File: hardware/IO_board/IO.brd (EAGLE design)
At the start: 167.9 x 122.5 mm, 73 parts, among them IC1 MAX232, IC10 74HCT245DW, IC11 74LVC1G08DBV, IC4 74HCT139N, IC5 74AC06N, IC7 MAX232, IC8 74HCT245DW, IC9 74HCT245DW, J1 DIN5, T1 BC847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

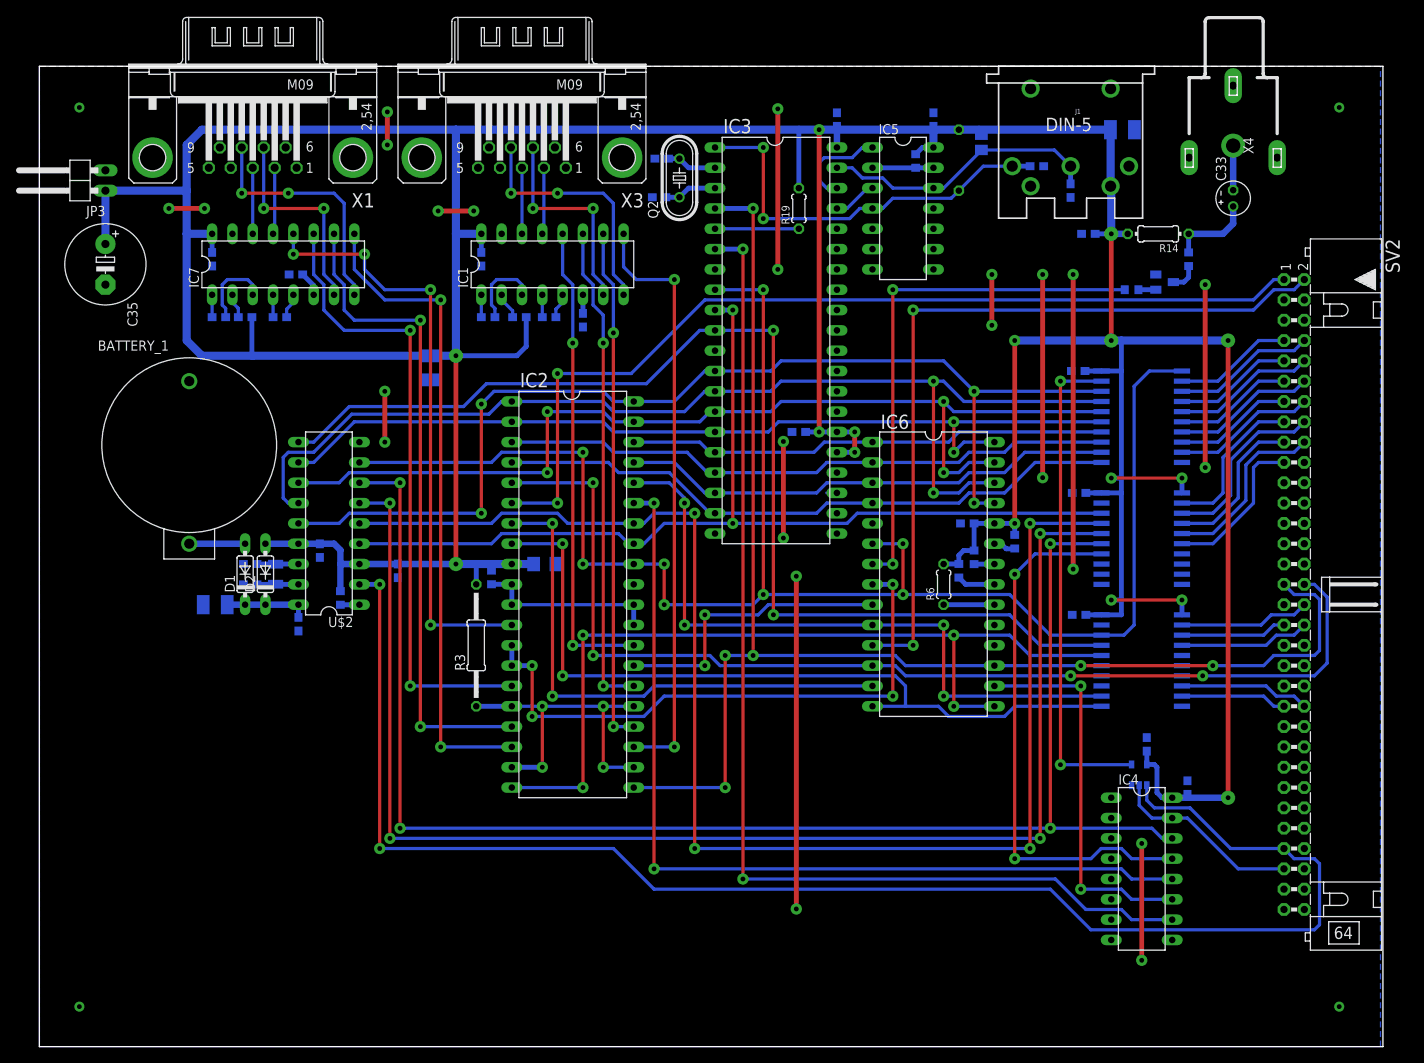
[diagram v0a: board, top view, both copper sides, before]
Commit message: Separate baudrate generator on I/O board
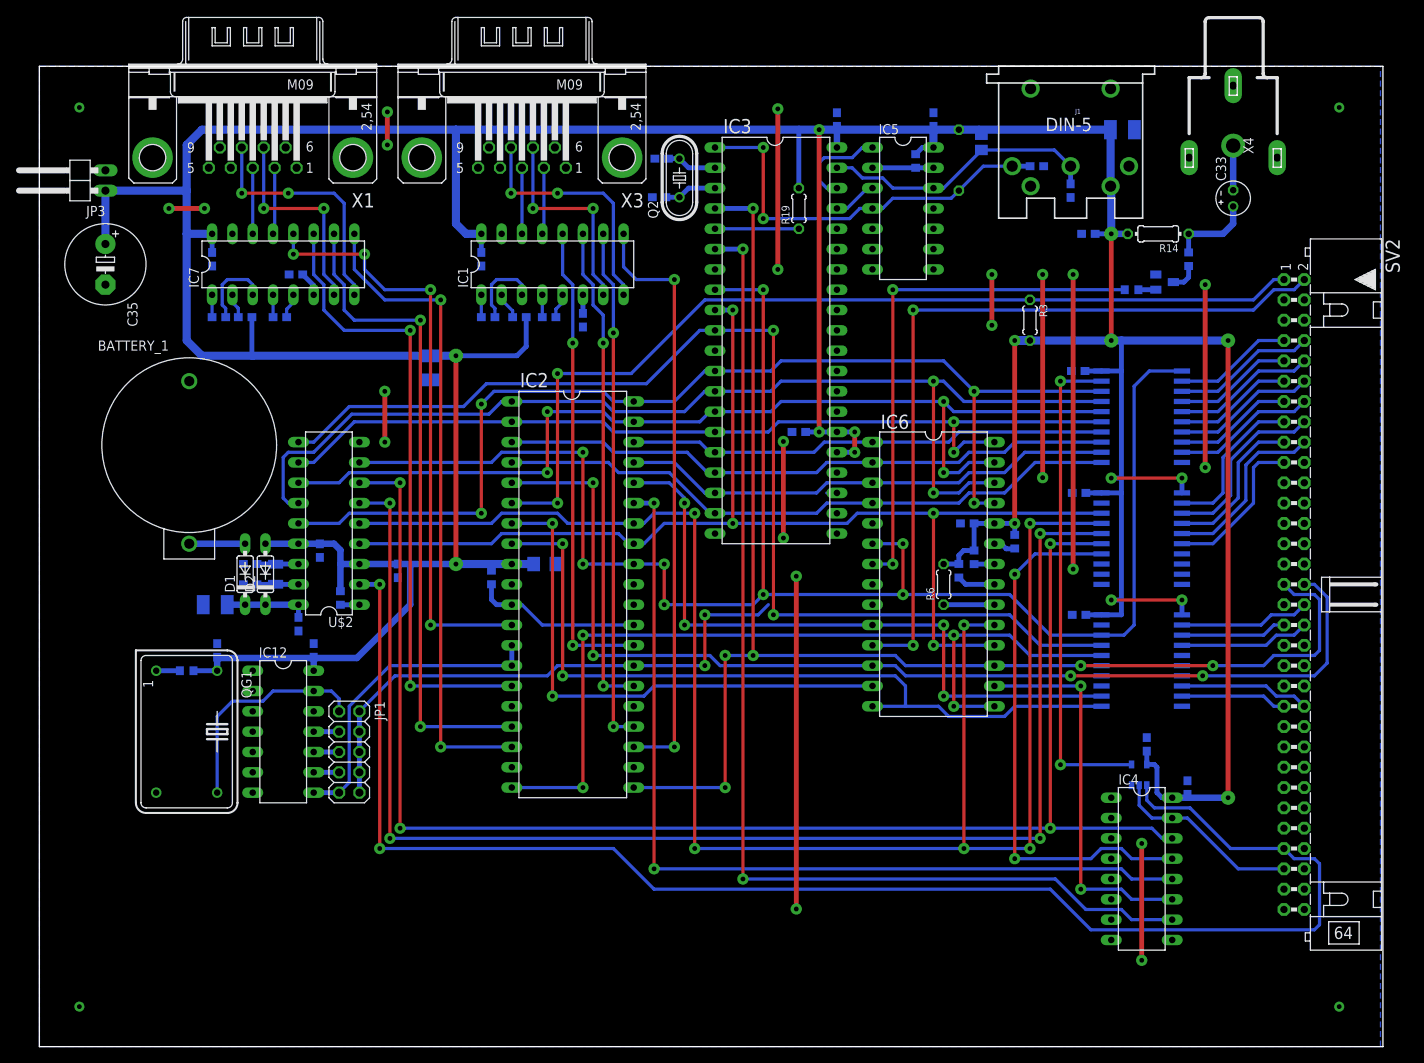
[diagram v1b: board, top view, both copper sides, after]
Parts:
- added C36, C37: 100N, rcl:C0603
- added IC12: 74HCT393N, 74xx-eu:DIL14
- added JP1: (no value), pinhead:2X05
- added QG1: (no value), crystal:DIL14S
- added R12: (no value), rcl:R0603
- R3: device rcl:0207/15 -> rcl:0204/5
- moved R3 80.3 mm to (123.8, 90.8), turned to 270 degrees
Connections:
- removed net BAUDRATE_A: IC2.13, IC2.14, IC6.8
- new net 1228800HZ: IC12.11, JP1.3
- new net 153600HZ: IC12.8, IC2.13, IC2.14, JP1.9
- new net 2457600HZ: IC12.13, JP1.1, QG1.8
- new net 307200HZ: IC12.9, JP1.7
- new net 614400HZ: IC12.10, JP1.5
- net A0: now also IC6.18
- net A1: now also IC6.19
- net BAUDRATE_B: now also JP1.10, JP1.2, JP1.4, JP1.6, JP1.8; no longer IC6.9
- net GND: now also C36.2, C37.2, IC12.1, IC12.12, IC12.2, IC12.7, IC2.19, IC2.22, QG1.7
- net IEI: now also R3.1
- net N$34: now also QG1.1, R12.2; no longer IC2.16, IC2.19, IC2.22, IC2.25, R3.1
- net N$36: no longer IC2.10, IC2.30
- net VCC: now also C36.1, C37.1, IC12.14, QG1.14, R12.1
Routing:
- net BAUDRATE_A: track 74.1 -> 0.00 mm, vias 4 -> 0
- net N$34: track 42.5 -> 2.96 mm, vias 4 -> 0
- net 153600HZ: track 0.00 -> 39.5 mm
- net BAUDRATE_B: track 36.7 -> 70.5 mm
- net A1: track 176.9 -> 208.6 mm, vias 4 -> 6
- net 2457600HZ: track 0.00 -> 28.1 mm
- net A0: track 124.3 -> 148.4 mm, vias 2 -> 4
- net VCC: track 622.2 -> 643.9 mm
- net GND: track 199.1 -> 194.7 mm, vias 24 -> 22
- net 614400HZ: track 0.00 -> 3.18 mm
- net 307200HZ: track 0.00 -> 3.18 mm
- net 1228800HZ: track 0.00 -> 3.18 mm
- net N$36: track 22.9 -> 21.0 mm

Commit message: I/O board: 0R resistors added to set baudrate at DART channel A
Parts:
- added R13: (no value), rcl:R0603
- added R16, R17, R18, R20, R21: 0R, rcl:R0603
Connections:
- new net BAUDRATE_A: IC2.13, IC2.14, R16.2, R17.2, R18.2, R20.2, R21.2
- new net N$41: IC12.2, R13.2
- net 1228800HZ: now also R17.1
- net 153600HZ: now also R21.1; no longer IC2.13, IC2.14
- net 2457600HZ: now also R16.1
- net 307200HZ: now also R20.1
- net 614400HZ: now also R18.1
- net GND: no longer IC12.2
- net VCC: now also R13.1
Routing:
- net BAUDRATE_A: track 0.00 -> 55.0 mm
- net 153600HZ: track 39.5 -> 5.18 mm
- net GND: track 194.7 -> 202.3 mm, vias 22 -> 24
- net N$41: track 0.00 -> 5.41 mm
- net 614400HZ: track 3.18 -> 5.18 mm
- net 307200HZ: track 3.18 -> 5.18 mm
- net 1228800HZ: track 3.18 -> 5.18 mm
- net 2457600HZ: track 28.1 -> 28.6 mm
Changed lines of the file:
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@@
 <element name="C37" library="rcl" package="C0603" value="100N" x="34.29" y="49.53" rot="MR90"/>
 <element name="R12" library="rcl" package="R0603" value="" x="18.415" y="46.99" rot="MR0"/>
+<element name="R13" library="rcl" package="R0603" value="" x="31.115" y="47.625" rot="MR270"/>
+<element name="R17" library="rcl" package="R0603" value="0R" x="31.4325" y="39.37" rot="MR0"/>
+<element name="R18" library="rcl" package="R0603" value="0R" x="31.4325" y="36.83" rot="MR0"/>
+<element name="R20" library="rcl" package="R0603" value="0R" x="31.4325" y="34.29" rot="MR0"/>
+<element name="R21" library="rcl" package="R0603" value="0R" x="31.4325" y="31.75" rot="MR0"/>
+<element name="R16" library="rcl" package="R0603" value="0R" x="38.1" y="44.45" rot="MR180"/>
 </elements>
 <signals>
@@
 <contactref element="IC12" pad="7"/>
 <contactref element="IC12" pad="12"/>
-<contactref element="IC12" pad="2"/>
 <contactref element="QG1" pad="7"/>
 <contactref element="IC12" pad="1"/>
 <contactref element="C36" pad="2"/>
 <contactref element="C37" pad="2"/>
+<via x="53.975" y="50.165" extent="1-16" drill="0.6" diameter="1.4224" shape="octagon"/>
+<via x="53.975" y="42.545" extent="1-16" drill="0.6" diameter="1.4224" shape="octagon"/>
+<wire x1="53.975" y1="50.165" x2="53.975" y2="42.545" width="0.6096" layer="1"/>
 </signal>
 <signal name="N$37">
@@
 <contactref element="C28" pad="1"/>
 <contactref element="C27" pad="2"/>
-<contactref element="IC2" pad="9"/>
 <wire x1="52.07" y1="114.6175" x2="52.07" y2="102.87" width="1.016" layer="16"/>
 <via x="52.07" y="86.36" extent="1-16" drill="0.6" diameter="1.778" shape="octagon"/>
 <wire x1="52.07" y1="86.36" x2="52.07" y2="60.325" width="0.6096" layer="1"/>
 <via x="52.07" y="60.325" extent="1-16" drill="0.6" diameter="1.778" shape="octagon"/>
-<wire x1="59.055" y1="60.325" x2="56.515" y2="60.325" width="1.016" layer="16"/>
 <wire x1="52.07" y1="60.325" x2="56.515" y2="60.325" width="1.016" layer="16"/>
 <contactref element="IC6" pad="24"/>
-<wire x1="59.055" y1="60.325" x2="61.7825" y2="60.325" width="1.016" layer="16"/>
 <wire x1="99.695" y1="114.6175" x2="111.76" y2="114.6175" width="1.016" layer="16"/>
 <wire x1="111.76" y1="114.6175" x2="114.935" y2="114.6175" width="1.016" layer="16"/>
@@
 <contactref element="QG1" pad="14"/>
 <wire x1="34.29" y1="46.99" x2="34.29" y2="48.5775" width="0.8128" layer="16"/>
-<wire x1="34.29" y1="48.5775" x2="22.225" y2="48.5775" width="0.8128" layer="16"/>
+<wire x1="34.29" y1="48.5775" x2="31.115" y2="48.5775" width="0.8128" layer="16"/>
+<wire x1="31.115" y1="48.5775" x2="22.225" y2="48.5775" width="0.8128" layer="16"/>
 <wire x1="22.225" y1="48.5775" x2="22.225" y2="46.99" width="0.8128" layer="16"/>
 <wire x1="34.29" y1="48.5775" x2="39.6875" y2="48.5775" width="0.8128" layer="16"/>
@@
 <wire x1="22.225" y1="48.5775" x2="22.225" y2="48.68" width="0.6096" layer="16"/>
 <wire x1="34.29" y1="48.5775" x2="34.29" y2="48.68" width="0.6096" layer="16"/>
+<contactref element="R13" pad="1"/>
+<wire x1="31.115" y1="48.475" x2="31.115" y2="48.5775" width="0.4064" layer="16"/>
+<contactref element="IC2" pad="9"/>
+<wire x1="56.515" y1="60.325" x2="59.055" y2="60.325" width="1.016" layer="16"/>
+<wire x1="59.055" y1="60.325" x2="61.7825" y2="60.325" width="1.016" layer="16"/>
 </signal>
 <signal name="INT">
@@
 <signal name="153600HZ">
 <contactref element="IC12" pad="8"/>
-<contactref element="IC2" pad="13"/>
-<contactref element="IC2" pad="14"/>
 <contactref element="JP1" pad="9"/>
 <wire x1="34.29" y1="31.75" x2="37.465" y2="31.75" width="0.6096" layer="16"/>
-<wire x1="37.465" y1="31.75" x2="38.735" y2="33.02" width="0.4064" layer="16"/>
-<wire x1="38.735" y1="33.02" x2="38.735" y2="42.545" width="0.4064" layer="16"/>
-<wire x1="59.055" y1="47.625" x2="59.055" y2="50.165" width="0.6096" layer="16"/>
-<wire x1="59.055" y1="47.625" x2="43.815" y2="47.625" width="0.4064" layer="16"/>
-<wire x1="43.815" y1="47.625" x2="38.735" y2="42.545" width="0.4064" layer="16"/>
+<contactref element="R21" pad="1"/>
+<wire x1="32.2825" y1="31.75" x2="34.29" y2="31.75" width="0.6096" layer="16"/>
 </signal>
 <signal name="1228800HZ">
@@
 <contactref element="JP1" pad="3"/>
 <wire x1="34.29" y1="39.37" x2="37.465" y2="39.37" width="0.6096" layer="16"/>
+<contactref element="R17" pad="1"/>
+<wire x1="32.2825" y1="39.37" x2="34.29" y2="39.37" width="0.6096" layer="16"/>
 </signal>
 <signal name="614400HZ">
@@
 <contactref element="JP1" pad="5"/>
 <wire x1="34.29" y1="36.83" x2="37.465" y2="36.83" width="0.6096" layer="16"/>
+<contactref element="R18" pad="1"/>
+<wire x1="32.2825" y1="36.83" x2="34.29" y2="36.83" width="0.6096" layer="16"/>
 </signal>
 <signal name="307200HZ">
@@
 <contactref element="JP1" pad="7"/>
 <wire x1="34.29" y1="34.29" x2="37.465" y2="34.29" width="0.6096" layer="16"/>
+<contactref element="R20" pad="1"/>
+<wire x1="32.2825" y1="34.29" x2="34.29" y2="34.29" width="0.6096" layer="16"/>
 </signal>
 <signal name="2457600HZ">
@@
 <wire x1="29.21" y1="44.45" x2="34.29" y2="44.45" width="0.4064" layer="16"/>
 <contactref element="JP1" pad="1"/>
-<wire x1="34.29" y1="44.45" x2="36.5125" y2="44.45" width="0.4064" layer="16"/>
-<wire x1="36.5125" y1="44.45" x2="37.465" y2="43.4975" width="0.4064" layer="16"/>
-<wire x1="37.465" y1="43.4975" x2="37.465" y2="41.91" width="0.4064" layer="16"/>
+<wire x1="34.29" y1="44.45" x2="37.25" y2="44.45" width="0.4064" layer="16"/>
+<wire x1="37.465" y1="44.45" x2="37.465" y2="41.91" width="0.4064" layer="16"/>
+<contactref element="R16" pad="1"/>
+<wire x1="37.465" y1="44.45" x2="37.25" y2="44.45" width="0.4064" layer="16"/>
 </signal>
 <signal name="N$34">
@@
 <wire x1="14.605" y1="46.99" x2="17.565" y2="46.99" width="0.6096" layer="16"/>
 </signal>
+<signal name="N$41">
+<contactref element="IC12" pad="2"/>
+<contactref element="R13" pad="2"/>
+<wire x1="29.9475" y1="46.775" x2="27.6225" y2="44.45" width="0.4064" layer="16"/>
+<wire x1="27.6225" y1="44.45" x2="26.67" y2="44.45" width="0.4064" layer="16"/>
+<wire x1="31.115" y1="46.775" x2="29.9475" y2="46.775" width="0.4064" layer="16"/>
+</signal>
+<signal name="BAUDRATE_A">
+<contactref element="R21" pad="2"/>
+<contactref element="R17" pad="2"/>
+<contactref element="R18" pad="2"/>
+<contactref element="R20" pad="2"/>
+<wire x1="30.5825" y1="39.37" x2="30.5825" y2="36.83" width="0.6096" layer="16"/>
+<wire x1="30.5825" y1="36.83" x2="30.5825" y2="34.29" width="0.6096" layer="16"/>
+<wire x1="30.5825" y1="34.29" x2="30.5825" y2="31.75" width="0.6096" layer="16"/>
+<contactref element="IC2" pad="14"/>
+<contactref element="IC2" pad="13"/>
+<wire x1="59.055" y1="47.625" x2="44.1325" y2="47.625" width="0.4064" layer="16"/>
+<wire x1="38.735" y1="31.115" x2="37.7825" y2="30.1625" width="0.4064" layer="16"/>
+<wire x1="37.7825" y1="30.1625" x2="31.115" y2="30.1625" width="0.4064" layer="16"/>
+<wire x1="31.115" y1="30.1625" x2="30.5825" y2="30.695" width="0.4064" layer="16"/>
+<wire x1="30.5825" y1="31.75" x2="30.5825" y2="30.695" width="0.4064" layer="16"/>
+<wire x1="59.055" y1="47.625" x2="59.055" y2="50.165" width="0.6096" layer="16"/>
+<wire x1="38.735" y1="44.45" x2="38.735" y2="31.115" width="0.4064" layer="16"/>
+<contactref element="R16" pad="2"/>
+<wire x1="38.735" y1="44.45" x2="38.95" y2="44.45" width="0.4064" layer="16"/>
+<wire x1="38.95" y1="44.45" x2="40.9575" y2="44.45" width="0.4064" layer="16"/>
+<wire x1="40.9575" y1="44.45" x2="44.1325" y2="47.625" width="0.4064" layer="16"/>
+</signal>
 </signals>
